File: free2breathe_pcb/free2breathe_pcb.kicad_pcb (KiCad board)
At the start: 2 copper layers, 108.5 x 115 mm, 96 parts, among them J1 USB4110-GF-A_REVB, J2 LED_Connector, J3 Alarm_Connector, Q1 AO3401A, Q2 DMN3404L, SW1 Power_Switch, U1 IP5328, U2 MCP6044-E/P, U3 MCP6044-E/P, U4 SO2 Sensor, U5 CO Sensor, U6 MCP6044-E/P, U7 O3 Sensor, U8 MCP6044-E/P, U9 NO2 Sensor

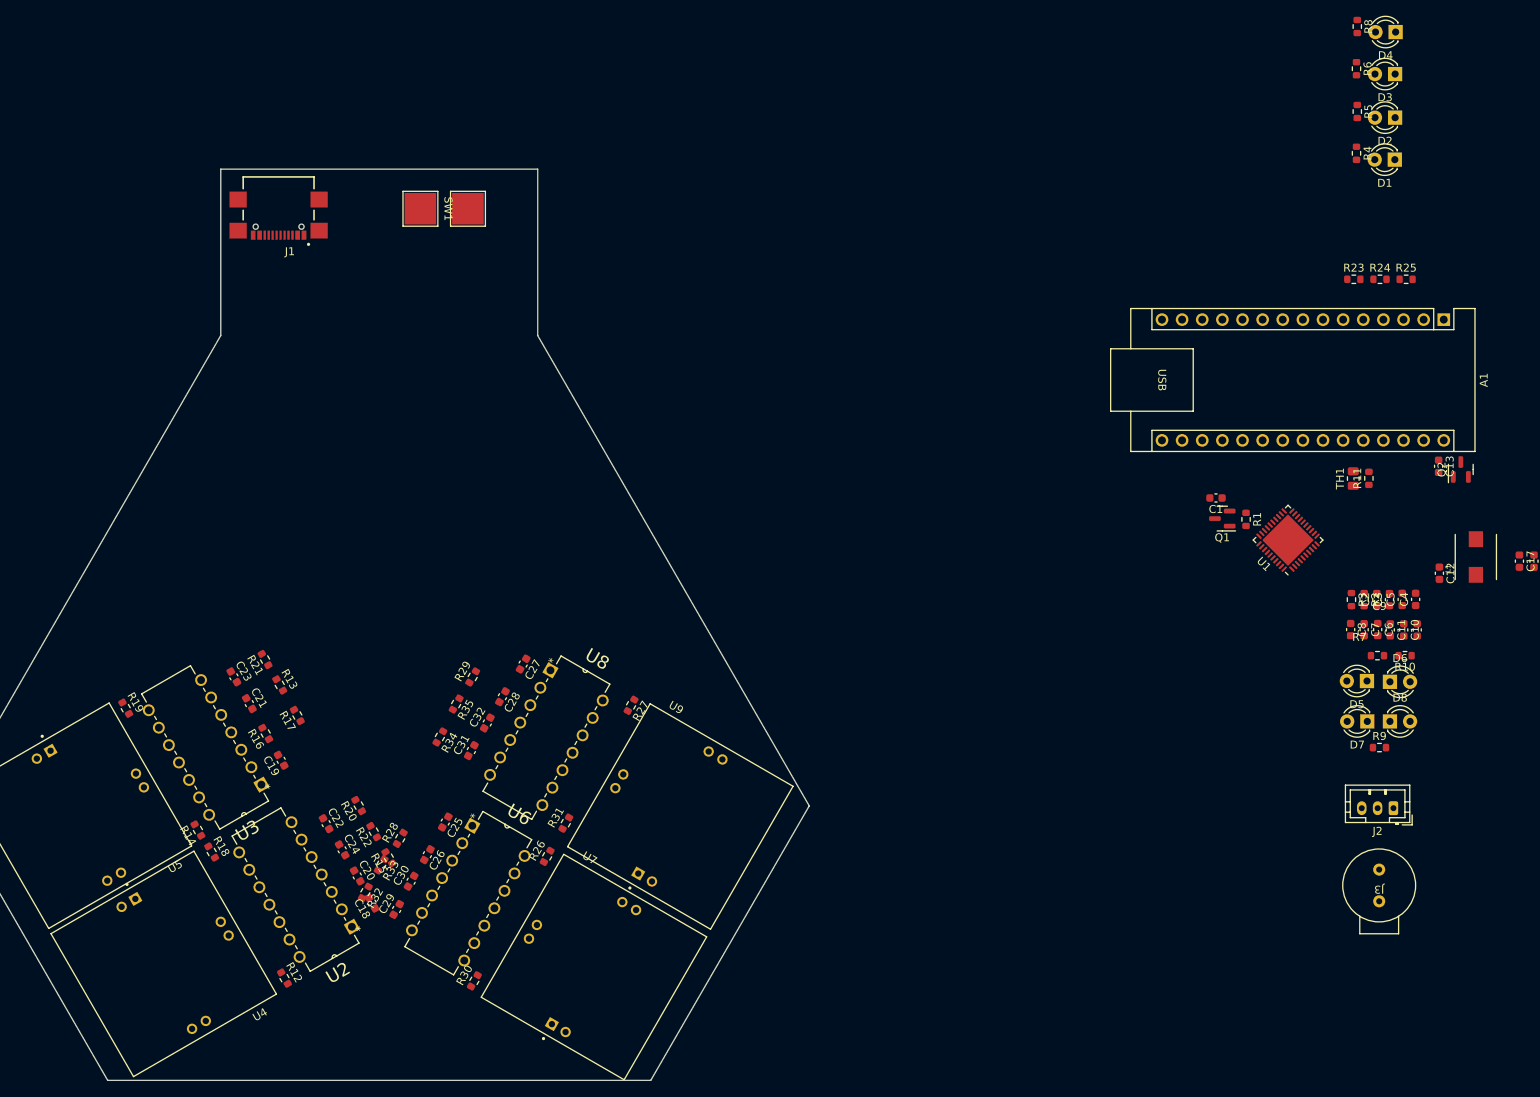
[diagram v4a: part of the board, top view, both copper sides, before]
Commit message: initial arrangement for new layout, add mounting holes
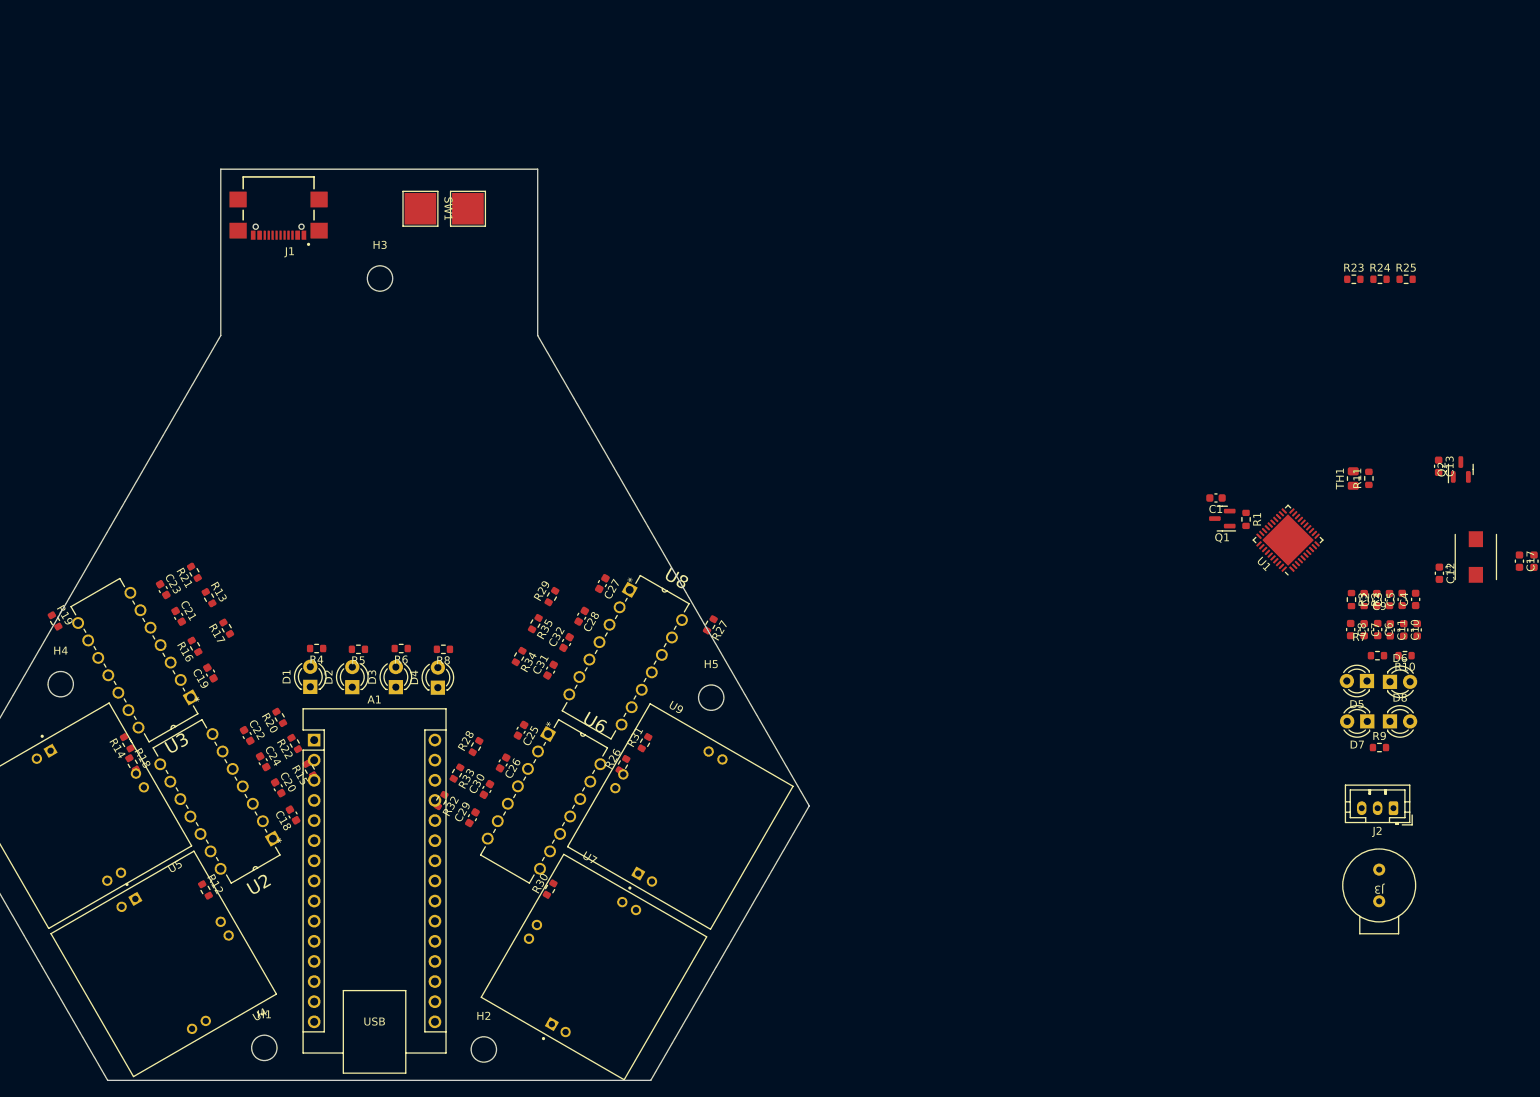
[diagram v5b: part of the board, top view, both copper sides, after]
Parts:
- added H1: MountingHole_Pad, MountingHole:MountingHole_3.2mm_M3, F.Cu at (105.5, 160.9)
- added H2: MountingHole_Pad, MountingHole:MountingHole_3.2mm_M3, F.Cu at (133.2, 161.1)
- added H3: MountingHole_Pad, MountingHole:MountingHole_3.2mm_M3, F.Cu at (120.1, 63.8)
- added H4: MountingHole_Pad, MountingHole:MountingHole_3.2mm_M3, F.Cu at (79.8, 115.0)
- added H5: MountingHole_Pad, MountingHole:MountingHole_3.2mm_M3, F.Cu at (161.9, 116.7)
- moved D1 152.2 mm to (111.3, 115.3), turned to 90 degrees
- moved A1 152.1 mm to (111.8, 122.0), turned to 0 degrees
- moved D2 150.0 mm to (116.6, 115.4), turned to 90 degrees
- moved D3 148.0 mm to (122.1, 115.4), turned to 90 degrees
- moved D4 146.5 mm to (127.4, 115.4), turned to 90 degrees
- moved R4 145.4 mm to (112.1, 110.5), turned to 180 degrees
- moved R5 143.2 mm to (117.4, 110.6), turned to 180 degrees
- moved R6 141.0 mm to (122.8, 110.5), turned to 180 degrees
- moved R8 139.6 mm to (128.1, 110.6), turned to 180 degrees
- moved C26 15.0 mm to (135.6, 124.9)
- moved R28 15.0 mm to (132.2, 122.9)
- moved C29 15.0 mm to (131.8, 131.9)
- moved C30 15.0 mm to (133.6, 128.3)
- moved R30 15.0 mm to (141.6, 140.9)
- moved R32 15.0 mm to (127.8, 129.7)
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
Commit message: further refinement
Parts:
- J2: footprint Connector_JST:JST_PH_B3B-PH-K_1x03_P2.00mm_Vertical -> Connector_JST:JST_PH_S3B-PH-K_1x03_P2.00mm_Horizontal
- moved BT2 183.4 mm to (91.1, 93.6), turned to -30 degrees
- moved C9 152.1 mm to (102.7, 74.4), turned to 90 degrees
- moved C4 150.2 mm to (102.9, 78.2), turned to -90 degrees
- moved C10 148.8 mm to (104.4, 74.4), turned to 90 degrees
- moved C5 146.8 mm to (104.6, 78.2), turned to -90 degrees
- moved C11 145.5 mm to (106.1, 74.4), turned to 90 degrees
- moved C3 143.7 mm to (106.2, 78.2), turned to -90 degrees
- moved C6 142.4 mm to (107.7, 74.3), turned to 90 degrees
- moved C2 140.5 mm to (107.8, 78.2), turned to -90 degrees
- moved C7 139.1 mm to (109.4, 74.4), turned to 90 degrees
- moved R2 137.4 mm to (109.4, 78.2), turned to 90 degrees
- moved R7 136.2 mm to (112.4, 85.1)
- moved C8 135.7 mm to (111.1, 74.4), turned to 90 degrees
- moved R10 135.0 mm to (117.0, 85.1)
- moved BT3 134.9 mm to (139.7, 78.3), turned to 30 degrees
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
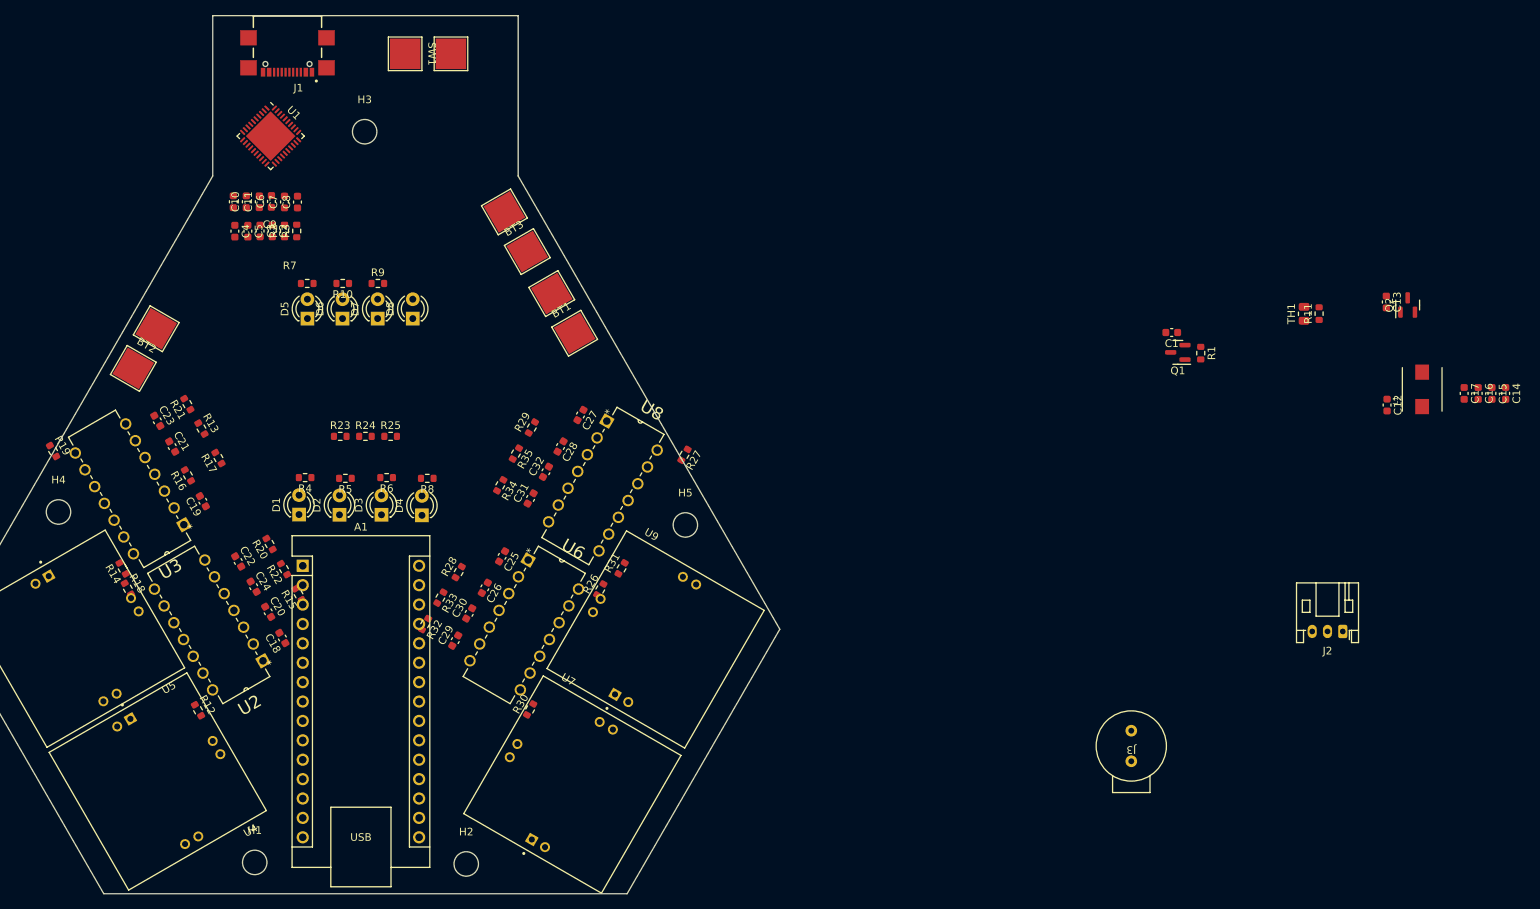
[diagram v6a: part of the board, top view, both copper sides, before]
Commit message: placed components, changed power LEDs
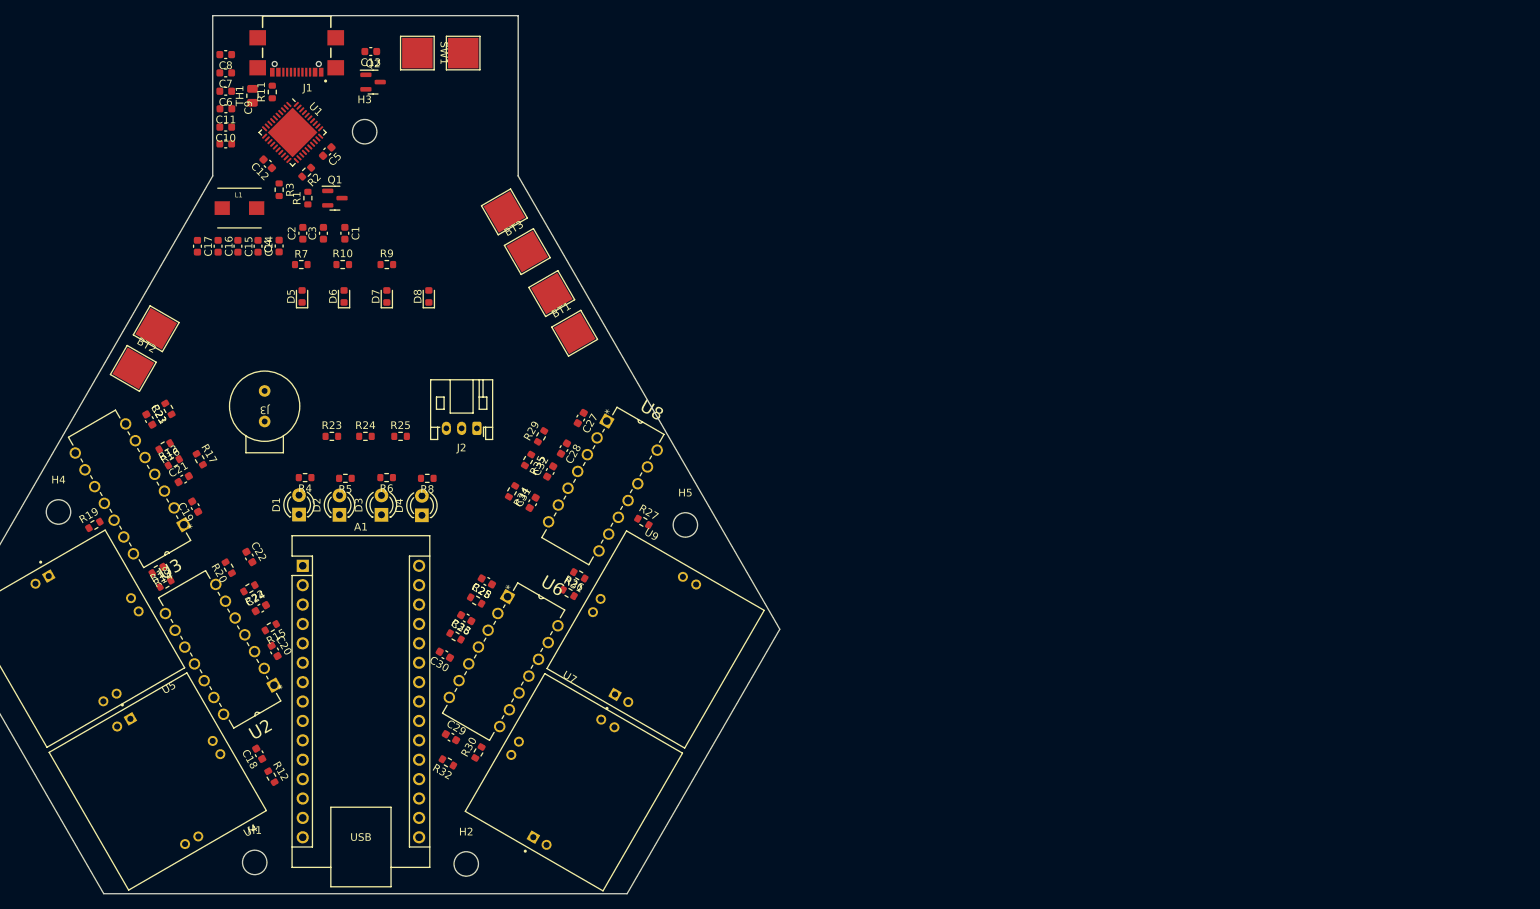
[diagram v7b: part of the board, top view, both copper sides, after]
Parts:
- D5, D6, D7, D8: footprint LED_THT:LED_D3.0mm -> LED_SMD:LED_0603_1608Metric
- moved C17 167.0 mm to (98.0, 80.2)
- moved C16 166.2 mm to (100.7, 80.2)
- moved C15 165.4 mm to (103.3, 80.2)
- moved C14 164.5 mm to (105.9, 80.2)
- moved L1 156.7 mm to (103.5, 75.2), turned to 0 degrees
- moved C12 150.0 mm to (107.2, 69.4), turned to 135 degrees
- moved TH1 140.7 mm to (105.2, 60.5)
- moved R11 140.1 mm to (107.8, 60.0)
- moved Q2 138.6 mm to (121.0, 58.7), turned to 0 degrees
- moved C13 137.0 mm to (120.7, 54.7), turned to 180 degrees
- moved J3 121.9 mm to (106.8, 101.2)
- moved R1 118.7 mm to (112.5, 73.9), turned to 90 degrees
- moved J2 116.5 mm to (134.6, 104.0)
- moved Q1 112.2 mm to (116.0, 73.9), turned to 0 degrees
- moved C1 109.1 mm to (117.3, 78.5), turned to -90 degrees
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
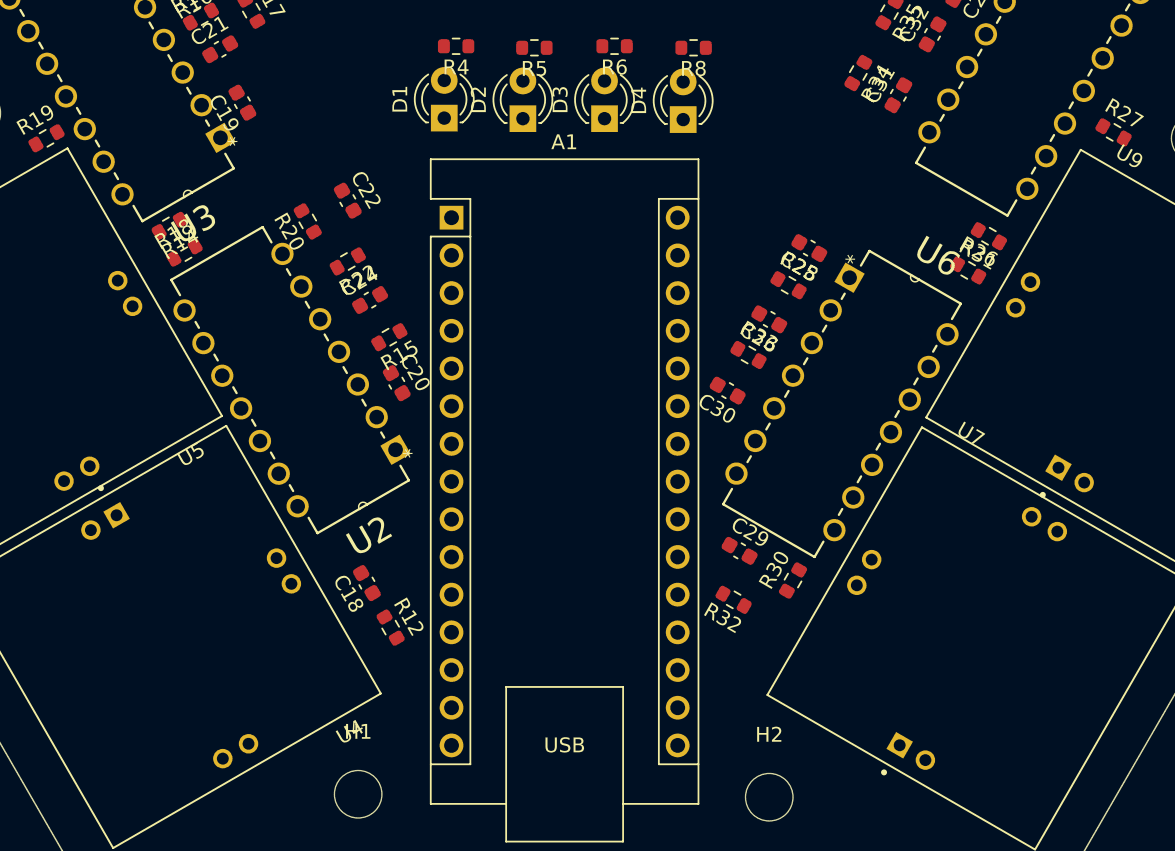
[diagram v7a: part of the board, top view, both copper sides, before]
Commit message: some routing done around the bottom sensors
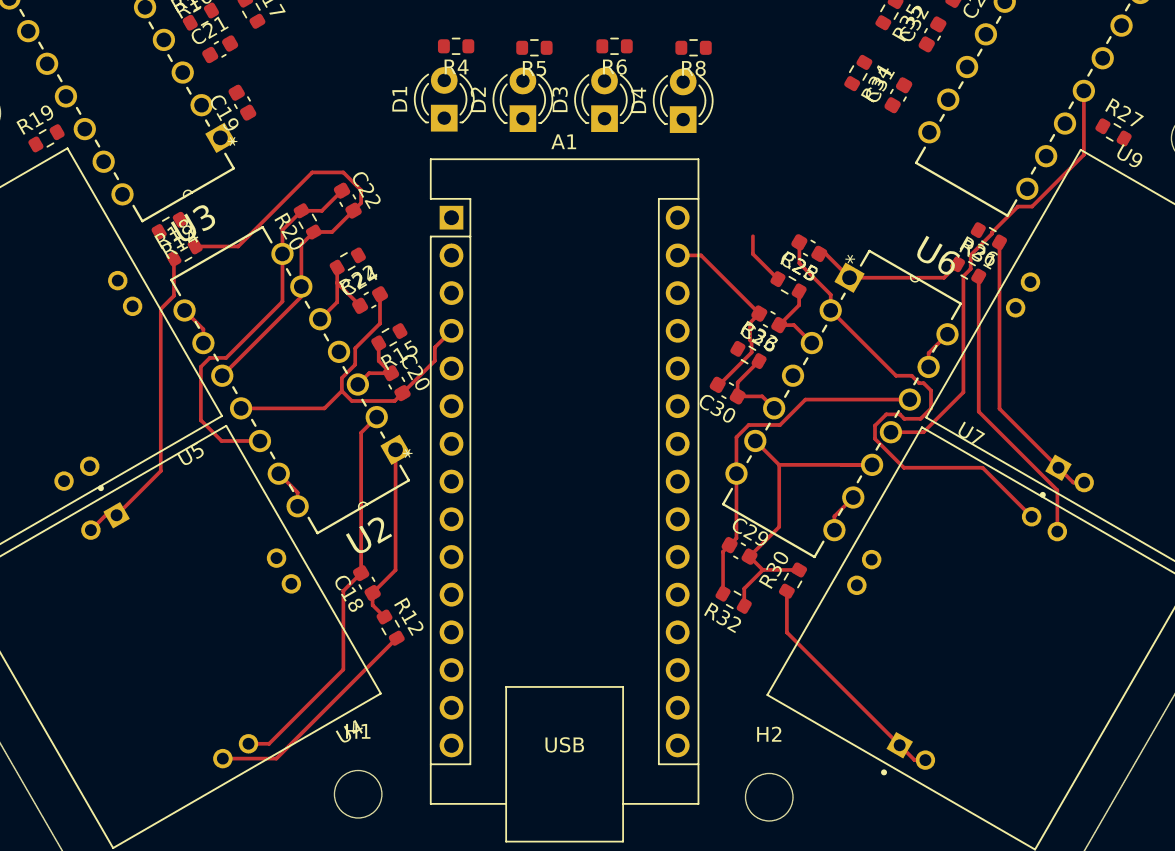
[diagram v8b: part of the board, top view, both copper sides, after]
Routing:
- net GND: track 0.00 -> 68.5 mm
- net Net-(C25-Pad2): track 0.00 -> 33.8 mm
- net Net-(C22-Pad2): track 0.00 -> 30.8 mm
- net Net-(C18-Pad2): track 0.00 -> 26.4 mm
- net Net-(C22-Pad1): track 0.00 -> 25.4 mm
- net Net-(C29-Pad2): track 0.00 -> 24.3 mm
- net Net-(C29-Pad1): track 0.00 -> 23.6 mm
- net Net-(R18-Pad1): track 0.00 -> 21.0 mm
- net Net-(R26-Pad2): track 0.00 -> 19.4 mm
- net Net-(R31-Pad1): track 0.00 -> 19.0 mm
- net Net-(R30-Pad1): track 0.00 -> 16.3 mm
- net Net-(R12-Pad2): track 0.00 -> 15.1 mm
- net Net-(C18-Pad1): track 0.00 -> 12.2 mm
- net Net-(C25-Pad1): track 0.00 -> 10.4 mm
- net Net-(C24-Pad1): track 0.00 -> 6.13 mm
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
